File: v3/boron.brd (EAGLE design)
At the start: 100 x 80 mm, 3 parts, among them U1 BQ24168RGET, U2 ATTINY84-20MU20M1-L

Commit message: Progress on Boron eval board.
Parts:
- removed U2: ATTINY84-20MU20M1-L, 32bits:20M1-L
- added C1, C3, C7, C8: 1uF, AVX_By_element14_Batch_1:CAPC1608X94N
- added C2, C6: 4.7uF, AVX_By_element14_Batch_1:CAPC2013X140N
- added C4: 47UF, AVX_By_element14_Batch_1:CAPCP7343X430N
- added C5: 10nF, AVX_By_element14_Batch_1:CAPC1608X90N
- added J1: batt, SparkFun-Connectors:JST-2-SMD
- added J10: USB_MINI-B_SMT, SparkFun-Connectors:USB-MINIB
- added J11: 5.5x2.1mm Barrel, SparkFun-Connectors:POWER_JACK_SMD
- added J12: out, SparkFun-Connectors:1X02_2.54_SCREWTERM
- added J13: debug, SparkFun-Connectors:2X3_SMT_POSTS
- added J4: ISP, SparkFun-Connectors:2X3_SMT_POSTS
- added L1: DR73-2R2-R, 32bits:DR73
- added L2: 1.0 uH, Bourns_By_element14_Batch_1:INDC3225X22N
- added Q1: Si7137DP, 32bits:SO-8
- added U2_C1: 10nF, Yageo_By_element14_Batch_1:CAPC1005X55N
- added U2_C2: 2.2uF, AVX_By_element14_Batch_1:CAPC1005X60N
- added U2_L1: 1 kOhm @ 100MHz, SparkFun-Resistors:0402
- added U2_R1, U2_R2: 10k, SparkFun-Resistors:0402
- added U2_R10, U2_R3, U2_R9, U6_RFBB: 100K Ohms, Vishay_By_element14_Batch_1:RESC1005X40N
- added U3: ATTINY84-20MU, 32bits:20M1
- added U6: TPS61230A, 32bits:VQFN7
- added U6_CBST: 10 nF, Kemet_By_element14_Batch_1:CAPC1005X60N
- added U6_CFF: 10pF, Kemet_By_element14_Batch_1:CAPC1608X85N
- added U6_CIN: 22uF, Murata_By_element14_Batch_1:CAPC2013X135N
- added U6_COUT: 22uF, Murata_By_element14_Batch_1:CAPC3225X270N
- added U6_RFBT: 316K Ohms, Vishay_By_element14_Batch_1:RESC1005X40N
- moved 5 10.9 mm to (2.54, 2.54)
- renumbered U1 to U9
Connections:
- removed net PGND: U9.17
- removed net PGND_2: U9.15
- removed net SGND: U9.16
- new net !RESET: J4.5, U3.13
- new net MISO: J4.1, U3.20
- new net MOSI/SDA: J4.4, U2_L1.1, U2_L1.2, U2_R1.2, U2_R3.2, U3.16
- new net MOT_6V: U3.4
- new net N$1: C2.1, U9.20
- new net N$2: J1.2, J13.5
- new net N$4: Q1.P$4, U9.10
- new net N$5: C4.2, U9.13, U9.14
- new net N$6: C6.1, U9.23
- new net N$8: C7.1, J10.VBUS, U9.22
- new net SCK: J4.3, U2_R10.2, U2_R2.1, U3.1
- new net SYS_5V: J12.P1, J4.2, U2_C1.2, U2_C2.2, U2_R10.1, U2_R3.1, U2_R9.1, U3.3, U3.9, U6.P$7, U6_CFF.2, U6_COUT.2, U6_RFBT.1
- new net U6_CBST: U6.P$1, U6_CBST.1
- new net U6_FB: U6.P$3, U6_CFF.1, U6_RFBB.1, U6_RFBT.2
- new net U6_SW: L2.1, U6.P$5, U6_CBST.2
- new net U9_BOOT: C5.1, U9.19
- new net U9_CD: J13.1, U9.24
- new net U9_DRV: C8.2, J13.3, U9.6, U9.9
- new net U9_IN: C1.1, J11.VIN0, U9.21
- new net U9_INT: U2_R9.2, U3.2, U9.7
- new net U9_SCL: U2_R2.2, U9.3
- new net U9_SDA: U2_R1.1, U9.4
- new net U9_STAT: U9.8
- new net U9_SW: C5.2, L1.1, U9.18
- new net VBAT: C3.1, J13.6, Q1.P$5, Q1.P$6, Q1.P$7, Q1.P$8, Q1.P$9, U3.5, U9.11, U9.12
- net GND: now also C1.2, C2.2, C3.2, C4.1, C6.2, C7.2, C8.1, J1.1, J10.GND, J11.P$4, J12.P2, J13.2, J4.6, U2_C1.1, U2_C2.1, U3.8, U6.P$6, U6_CIN.1, U6_COUT.1, U6_RFBB.2, U9.15, U9.16, U9.17, U9.25; no longer U2.8
- net VCC: now also L1.2, L2.2, Q1.P$1, Q1.P$2, Q1.P$3, U6.P$2, U6.P$4, U6_CIN.2; no longer U2.9

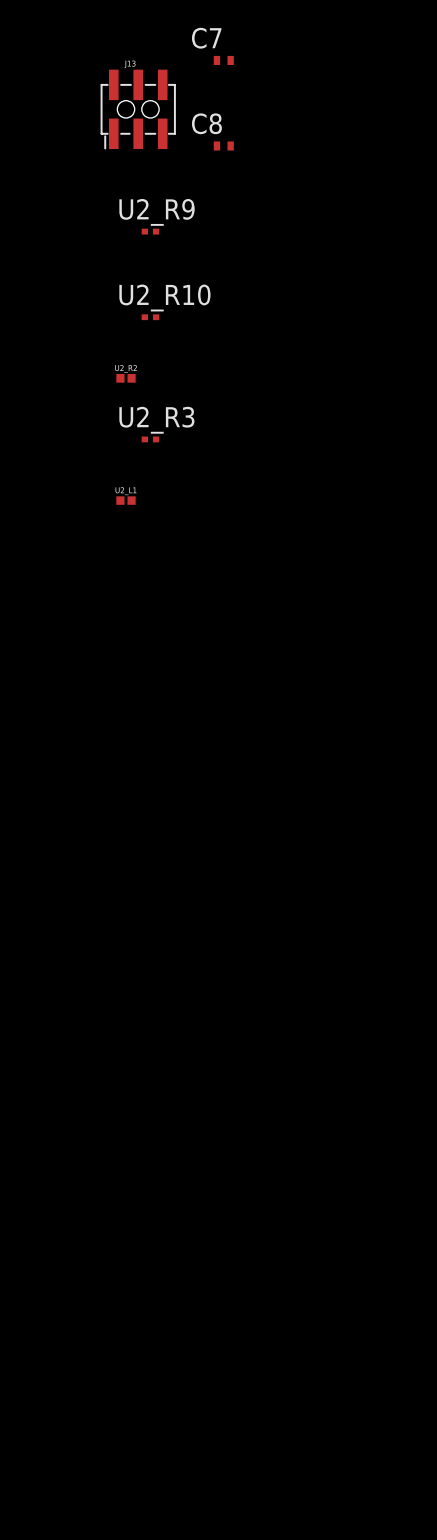
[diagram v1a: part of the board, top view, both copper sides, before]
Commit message: Schematic Complete.
Unless I go with a different 5V supply.
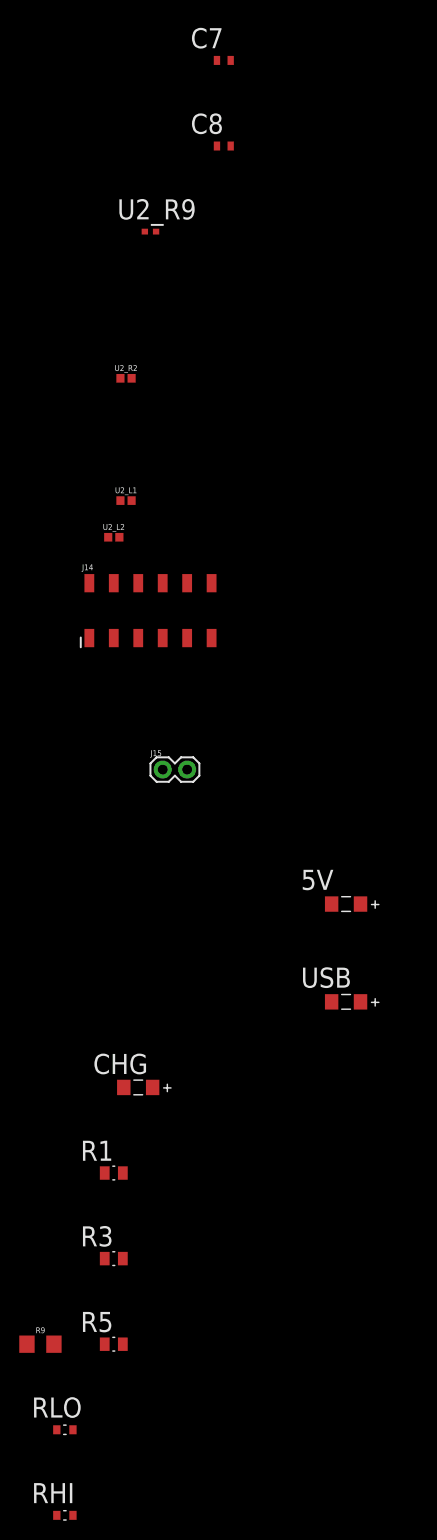
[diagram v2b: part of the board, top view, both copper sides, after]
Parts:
- removed J13: debug, SparkFun-Connectors:2X3_SMT_POSTS
- removed U2_R10, U2_R3: 100K Ohms, Vishay_By_element14_Batch_1:RESC1005X40N
- added 5V, USB: QTLP650C-4, Dialight_By_element14_Batch_1:LED_597-3311-407F
- added CHG: QTLP650C-7, Dialight_By_element14_Batch_1:LED_597-3111-407F
- added J14: debug, SparkFun-Connectors:2X6_SMD
- added J15: test, SparkFun-Connectors:1X02
- added R1, R3, R5: 150 Ohm, Panasonic_By_element14_Batch_1:RESC2013X65N
- added R9: (no value), 32bits:1206
- added RHI: 5.3K, Vishay_By_element14_Batch_1:RESC1608X60N
- added RLO: 11K, Vishay_By_element14_Batch_1:RESC1608X60N
- added U2_L2: 1 kOhm @ 100MHz, SparkFun-Resistors:0402
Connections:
- removed net MOT_6V: U3.4
- removed net N$8: C7.1, J10.VBUS, U9.22
- removed net SCK: J4.3, U2_R10.2, U2_R2.1, U3.1
- new net LA_5: 5V.2, R1.1
- new net LA_CHG: CHG.2, R3.1
- new net LA_USB: R5.1, USB.2
- new net N$3: U2_L2.2, U3.1
- new net U9_LOAD: J15.2, L1.2, Q1.P$1, Q1.P$2, Q1.P$3
- new net U9_PSEL: J14.9, U9.2
- new net U9_TS: R9.2, RHI.2, RLO.1, U9.9
- new net U9_USB: C7.1, J10.VBUS, R5.2, U9.22
- net GND: now also 5V.1, J14.10, J14.2, J14.6, R9.1, RLO.2, USB.1; no longer J13.2
- net MOSI/SDA: no longer J4.4, U2_L1.2, U2_R1.2, U2_R3.2
- net N$2: now also J14.11; no longer J13.5
- net SYS_5V: now also R1.2, U2_R1.1, U2_R2.1; no longer U2_R10.1, U2_R3.1
- net U9_CD: now also J14.1; no longer J13.1
- net U9_DRV: now also J14.3, J14.7, R3.2, RHI.1; no longer J13.3, U9.9
- net U9_SCL: now also J4.3, U2_L2.1
- net U9_SDA: now also J4.4, U2_L1.2, U2_R1.2; no longer U2_R1.1
- net U9_STAT: now also CHG.1
- net VBAT: now also J14.12; no longer J13.6
- net VCC: now also J15.1; no longer L1.2, Q1.P$1, Q1.P$2, Q1.P$3

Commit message: Good progress on Boron layout.
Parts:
- removed J15: test, SparkFun-Connectors:1X02
- added J13: RASM722, 32bits:RASM722
- added J16: 5V, SparkFun-Connectors:1X04
- added R2, R4: 1M Ohm, Vishay_By_element14_Batch_1:RESC1608X60N
- J11: value 5.5x2.1mm Barrel -> drv; device SparkFun-Connectors:POWER_JACK_SMD -> SparkFun-Connectors:1X04
- R9: value (none) -> 10K NTC
- RHI: value 5.3K -> 5.5K
- RLO: value 11K -> 11.6K
- moved RHI 405.2 mm to (52.4, 25.4), turned to 270 degrees
- moved R1 397.7 mm to (36.2, 58.4), turned to 180 degrees
- moved RLO 393.3 mm to (52.4, 21.9), turned to 270 degrees
- moved R9 388.9 mm to (57.1, 24.1), turned to 180 degrees
- moved R3 381.7 mm to (52.1, 29.2), turned to 180 degrees
- moved CHG 365.3 mm to (57.1, 29.2), turned to 180 degrees
- moved 5V 364.7 mm to (39.4, 56.8), turned to 90 degrees
- moved R5 360.2 mm to (8.89, 7.62)
- moved USB 321.3 mm to (3.81, 7.62)
- moved U2_L1 320.7 mm to (6.35, 55.9), turned to 135 degrees
- moved U2_L2 316.7 mm to (3.81, 48.3), turned to 45 degrees
- moved J14 314.5 mm to (45.7, 29.5), turned to 90 degrees
- moved U2_R2 312.1 mm to (14.0, 58.4), turned to 270 degrees
- moved U2_R9 295.7 mm to (8.89, 58.4), turned to 270 degrees
- moved C8 262.5 mm to (34.3, 29.2), turned to 270 degrees
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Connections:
- net MOSI/SDA renamed U3_PA6
- net N$1 renamed U9_PMIDI
- net N$2 renamed VBAT_CON
- net N$3 renamed U3_PA4
- net N$4 renamed U9_BGATE
- net N$6 renamed U9_PMIDU
- removed net N$5: C4.2, U9.13, U9.14
- removed net U9_LOAD: J15.2, L1.2, Q1.P$1, Q1.P$2, Q1.P$3
- new net ADC0: R2.1, U3.5
- new net ADC2: R4.1, U3.3
- new net GNDBREAK: J13.SHUNT
- new net U9_DRV_O: C8.2, J11.1, U9.6
- new net U9_SYS: C4.2, J16.1, L1.2, Q1.P$1, Q1.P$2, Q1.P$3, U9.13, U9.14
- net GND: now also J11.4, J13.SLEEVE, J16.4; no longer J11.P$4
- net SYS_5V: now also R4.2; no longer U3.3
- net U9_DRV: now also J11.2, J11.3; no longer C8.2, U9.6
- net U9_IN: now also J13.TIP; no longer J11.VIN0
- net VBAT: now also R2.2; no longer U3.5
- net VCC: now also J16.2, J16.3; no longer J15.1
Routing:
- net U9_USB: track 0.00 -> 42.4 mm
- net U9_TS: track 0.00 -> 29.5 mm, vias 0 -> 2
- net U9_STAT: track 0.00 -> 29.2 mm, vias 0 -> 2
- net U9_CD: track 0.00 -> 26.9 mm
- net U9_PSEL: track 0.00 -> 26.8 mm
- net VCC: track 0.00 -> 23.0 mm, vias 0 -> 3
- net U9_BGATE: track 0.00 -> 18.0 mm, vias 0 -> 2
- net U9_DRV: track 0.00 -> 14.8 mm
- net U9_BOOT: track 0.00 -> 10.4 mm, vias 0 -> 2
- net U9_DRV_O: track 0.00 -> 7.45 mm
- net U6_SW: track 0.00 -> 4.99 mm
- net VBAT_CON: track 0.00 -> 4.88 mm
- net U6_FB: track 0.00 -> 4.10 mm
- net U9_SYS: track 0.00 -> 3.87 mm
- net U9_PMIDI: track 0.00 -> 3.80 mm
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- added copper zone on layer 1, net SYS_5V
- added copper zone on layer 1, net U9_DRV
- added copper zone on layer 1, net U9_IN
- added copper zone on layer 1, net U9_SW
- added copper zone on layer 1, net U9_SYS
- added copper zone on layer 1, net VBAT
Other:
- outline, holes or cut-outs redrawn

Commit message: Boron off to OSH.
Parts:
- removed C4: 47UF, AVX_By_element14_Batch_1:CAPCP7343X430N
- removed C6: 4.7uF, AVX_By_element14_Batch_1:CAPC2013X140N
- removed L1: DR73-2R2-R, 32bits:DR73
- removed U2_C1: 10nF, Yageo_By_element14_Batch_1:CAPC1005X55N
- added U9_C4: 47uF, AVX_By_element14_Batch_1:CAPC3216X127N
- added U9_C6: 4.7uF, AVX_By_element14_Batch_1:CAPC2013X140N
- added U9_L1: DR73-2R2-R, 32bits:DR73
- J14: device SparkFun-Connectors:2X6_SMD -> SparkFun-Connectors:2X6
- J4: device SparkFun-Connectors:2X3_SMT_POSTS -> SparkFun-Connectors:2X3
- moved U2_C2 53.6 mm to (35.6, 10.2)
- moved U2_R2 52.4 mm to (26.7, 7.62), turned to 135 degrees
- moved U2_R9 51.9 mm to (27.9, 10.2), turned to 45 degrees
- moved U3 46.2 mm to (33.0, 12.7)
- moved U2_L1 45.9 mm to (30.5, 16.8)
- moved R4 45.5 mm to (29.2, 8.89)
- moved R2 45.1 mm to (30.5, 7.62)
- moved U2_R1 44.3 mm to (31.8, 19.1), turned to 225 degrees
- moved J4 43.9 mm to (22.9, 10.5), flipped to the top
- moved U2_L2 43.3 mm to (26.7, 11.4)
- moved J14 6.35 mm to (45.7, 23.2)
- moved 5 4.80 mm to (44.7, 5.08)
- moved J11 2.56 mm to (35.6, 25.7)
- moved J16 1.59 mm to (35.6, 46.0)
- moved C8 1.31 mm to (35.6, 28.9)
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- renumbered C2 to U9_C2, C5 to U9_C5
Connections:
- removed net U9_DRV_O: C8.2, J11.1, U9.6
- new net U9_DRV_0: J11.2, J11.3, U9.6
- net GND: now also U3.21, U9_C4.1, U9_C6.2; no longer C4.1, C6.2, U2_C1.1
- net SYS_5V: no longer U2_C1.2
- net U9_DRV: now also C8.2, J11.1; no longer J11.2, J11.3
- net U9_PMIDU: now also U9_C6.1; no longer C6.1
- net U9_SW: now also U9_L1.1; no longer L1.1
- net U9_SYS: now also U9_C4.2, U9_L1.2; no longer C4.2, L1.2
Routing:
- net SYS_5V: track 0.00 -> 83.8 mm, vias 0 -> 2
- net VBAT: track 2.62 -> 56.2 mm, vias 0 -> 1
- net U9_SCL: track 0.00 -> 27.2 mm
- net U9_SDA: track 0.00 -> 26.9 mm, vias 0 -> 1
- net U9_INT: track 0.00 -> 26.1 mm, vias 0 -> 2
- net GND: track 0.00 -> 18.9 mm, vias 0 -> 135
- net !RESET: track 0.00 -> 14.7 mm, vias 0 -> 1
- net U9_DRV: track 14.8 -> 29.5 mm
- net U9_DRV_0: track 0.00 -> 12.5 mm, vias 0 -> 1
- net MISO: track 0.00 -> 9.79 mm, vias 0 -> 1
- net U9_DRV_O: track 7.45 -> 0.00 mm
- net U3_PA4: track 0.00 -> 3.95 mm
- net ADC0: track 0.00 -> 2.95 mm
- net VBAT_CON: track 4.88 -> 7.75 mm
- net U9_CD: track 26.9 -> 24.2 mm, vias 0 -> 1
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- added copper zone on layer 1, net GND
- added copper zone on layer 16, net GND
- added copper zone on layer 1, net U9_USB
- removed copper zone on layer 1, net U9_DRV
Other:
- board size 100 x 80 mm -> 61 x 61 mm
- board text added: "BATT"
- board text added: "CD"
- board text added: "DRV"
- board text added: "GND"
- board text added: "PSEL"

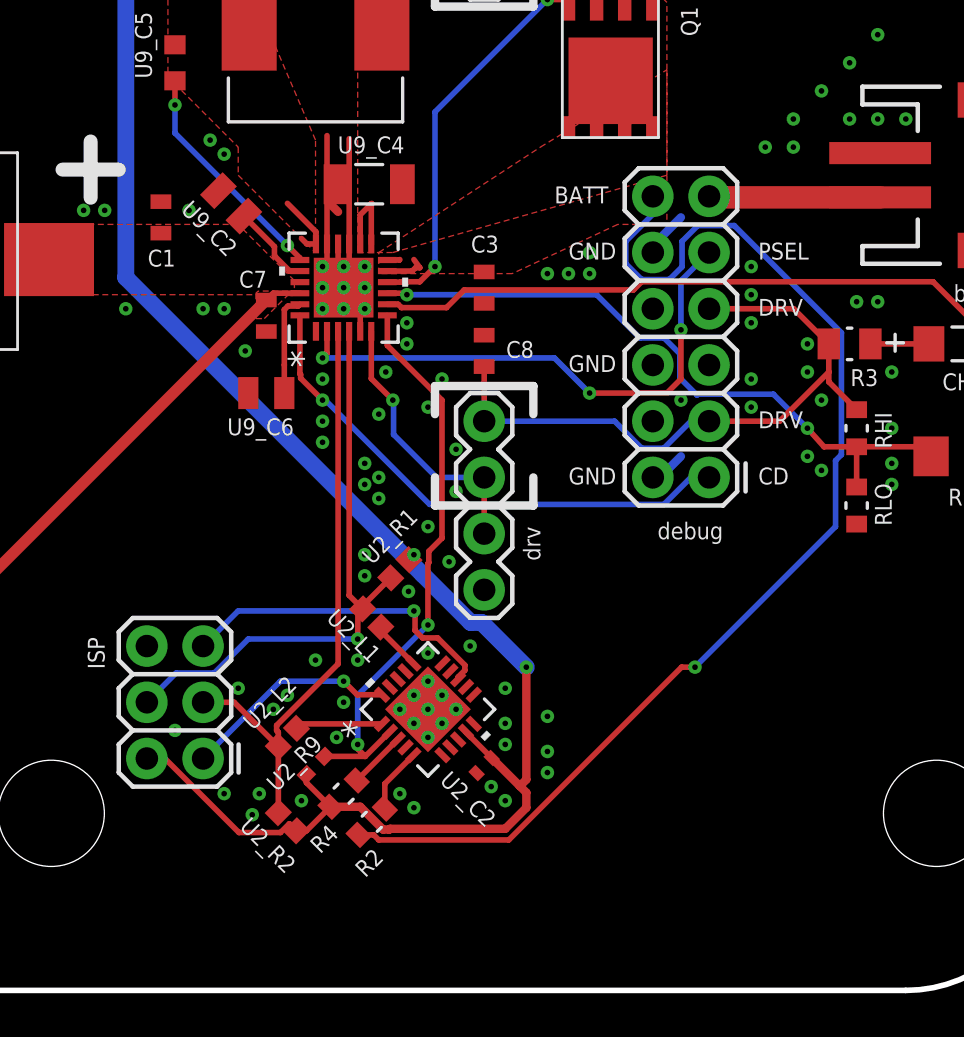
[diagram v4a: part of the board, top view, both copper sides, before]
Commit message: Boron R0 send to OSH part + NOTIFY.
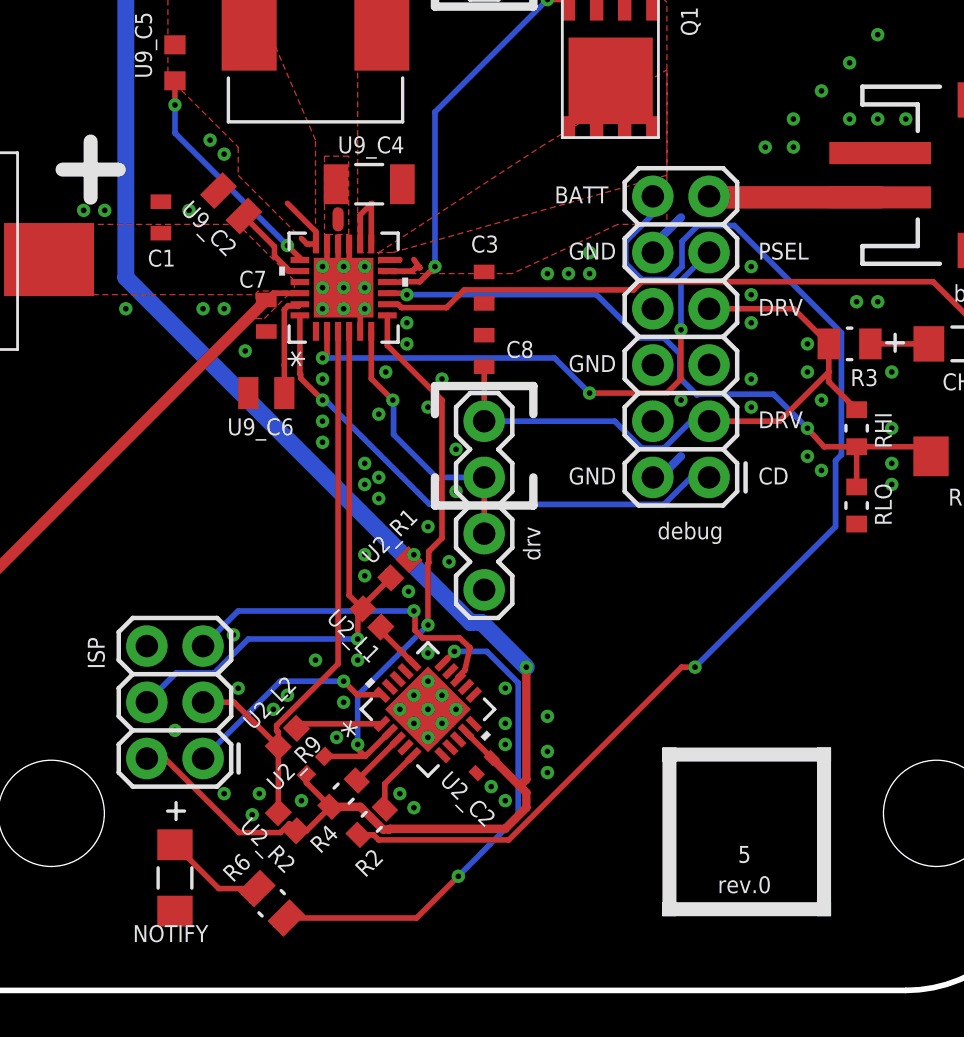
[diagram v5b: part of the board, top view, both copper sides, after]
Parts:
- added NOTIFY: QTLP650C-4, Dialight_By_element14_Batch_1:LED_597-3311-407F
- added R6: 150 Ohm, Panasonic_By_element14_Batch_1:RESC2013X65N
- moved 5 5.25 mm to (50.0, 4.62), flipped to the bottom
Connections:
- new net 1ROU: R6.2, U3.15
- new net LA_1: NOTIFY.2, R6.1
- net GND: now also NOTIFY.1
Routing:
- net 1ROU: track 0.00 -> 22.7 mm, vias 0 -> 2
- net GND: track 18.9 -> 9.69 mm
- net LA_1: track 0.00 -> 4.52 mm
- net !RESET: track 14.7 -> 15.4 mm

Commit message: Boron r.1 off to OSH park.
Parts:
- 5: value rev.0 -> rev.1
- moved U9_C4 0.32 mm to (30.4, 36.7)
- moved Q1 0.32 mm to (43.2, 44.8)
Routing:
- net U9_BGATE: track 17.9 -> 17.1 mm
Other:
- board text added: "D"
- board text added: "ENABLE"
- board text added: "G"
- board text added: "S"
